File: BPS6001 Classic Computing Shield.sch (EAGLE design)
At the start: 82 parts, among them IC1 MAX3232CSE, X1 VGA

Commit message: First outline of design moved to Eagle 9.
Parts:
- removed AJ1: AUDIO-CONNECTOR-6P-SMD-3440030P1, OPL Eagle Library:AUDIO-CONNECTOR-6P-SMD-3440030P1
- removed C4, C5, C6, C7: .1uF, GadgetFactory_6.0:C0805
- removed GROVE1: (no value), GadgetFactory_6.0:CONNECTOR_TWIG-2.0-LEADED
- removed IC1: MAX3232CSE, maxim:MAX3232CSE
- removed PS2_A: MINI-DIN6PTH, SparkFun-Connectors:MINI-DIN6PTH
- removed SP1: Serial Port, con-subd:M09HP
- added B1: SPARKFUN_LOGIC_LEVEL_CONVERTER, SparkFun-Boards:SPARKFUN_LOGIC_LEVEL_CONVERTER
- added R49, R50, R51: 1k, resistor:R-EU_R0603
- added X2: MAB6H, con-hirschmann:MAB6H
- C1, C2: value 4700pF -> 10p; device GadgetFactory:C0603 -> resistor:C-EUC0603; PARTNO C0603C472J5RACTU -> (none)
- C3: value .1uF -> 10p; device GadgetFactory_6.0:C0805 -> resistor:C-EUC0603; PARTNO GRM21BR71E104KA01L -> (none)
- R22, R28: value 3.3K -> 1k; device GadgetFactory:R0603 -> resistor:R-EU_R0603; PARTNO RMCF0603JT3K30 -> (none)
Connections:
- removed net 3V3: C7.1, CFG1.10, CFG1.2, CFG1.4, CFG1.6, CFG1.8, H1.3.3V, IC1P.VCC, R1A.2, R23A.2, R24A.2, R25A.2, R2A.2, R3A.2, R4A.2, R5A.2, R6A.2, R7A.2, R8A.2, S1.S1, S2.S1, S3.S1, S4.S1, S5.S1, SD1.VDD
- removed net AUDIO1-LEFT: H1.D28, R22A.2
- removed net AUDIO1-RIGHT: H1.D30, R28A.2
- removed net CTS: IC1G$1.R2OUT
- removed net DTE_CTS: IC1G$1.R2IN, SP1.8
- removed net DTE_RTS: IC1G$1.T2OUT, SP1.7
- removed net DTE_RX: IC1G$1.R1IN, SP1.2
- removed net DTE_TX: IC1G$1.T1OUT, SP1.3
- removed net N$12: C4.2, IC1G$1.C2+
- removed net N$13: C5.1, IC1G$1.C1-
- removed net N$14: C4.1, IC1G$1.C2-
- removed net N$2: AJ1.L, C1.1, R22A.1
- removed net N$34: AJ1.R, C2.1, R28A.1
- removed net N$6: C6.1, IC1G$1.V+
- removed net N$7: C3.1, IC1G$1.V-
- removed net N$8: C5.2, IC1G$1.C1+
- removed net PS2CLK1: H1.D5, PS2_A.5
- removed net PS2DAT1: H1.D4, PS2_A.1
- removed net RTS: IC1G$1.T2IN
- new net 3V3_PWR6: B1.LV, C3.2, CFG1.10, CFG1.2, CFG1.4, CFG1.6, CFG1.8, H1.3.3V, R1A.2, R23A.2, R24A.2, R25A.2, R2A.2, R3A.2, R4A.2, R5A.2, R6A.2, R7A.2, R8A.2, S1.S, S1.S1, S2.S, S2.S1, S3.S, S3.S1, S4.S, S4.S1, S5.S1, SD1.VDD
- new net 3V3_PWR7: PWR_2.3V3@P3
- new net IEC-H-ATN: B1.HV_TXO_1, C2.2, R28.1, X2.3
- new net IEC-H-CLK: B1.HV_RXI_1, R49.1, X2.4
- new net IEC-H-DATA: B1.HV_RXI_2, R50.1, X2.5
- new net IEC-H-RESET: B1.HV_TXO_2, R51.1, X2.6
- new net IEC-H-SRQ: R22.1, X2.1
- new net IEC-L-ATN: B1.LV_TXI_1, H1.D28
- new net IEC-L-CLK: B1.LV_RXO_1, H1.D4
- new net IEC-L-DATA: B1.LV_RXO_2, H1.D5
- new net IEC-L-RESET: B1.LV_TXI_2, H1.D30
- net 5V0: now also B1.HV, C1.1, R22.2, R28.2, R49.2, R50.2, R51.2; no longer GROVE1.3, PS2_A.4
- net GND: now also B1.GND, B1.GND@2, C2.1, C3.1, X2.2, X2.PE; no longer AJ1.COM1, AJ1.COM2, C2.2, C3.2, C6.2, C7.2, GROVE1.4, IC1P.GND, PS2_A.3, SP1.5, SP1.G1, SP1.G2
- net JS1_5: no longer GROVE1.2
- net JS1_9: no longer GROVE1.1
- net RX: no longer IC1G$1.R1OUT
- net TX: no longer IC1G$1.T1IN
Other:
- note removed: "Seeed Grove Connector"

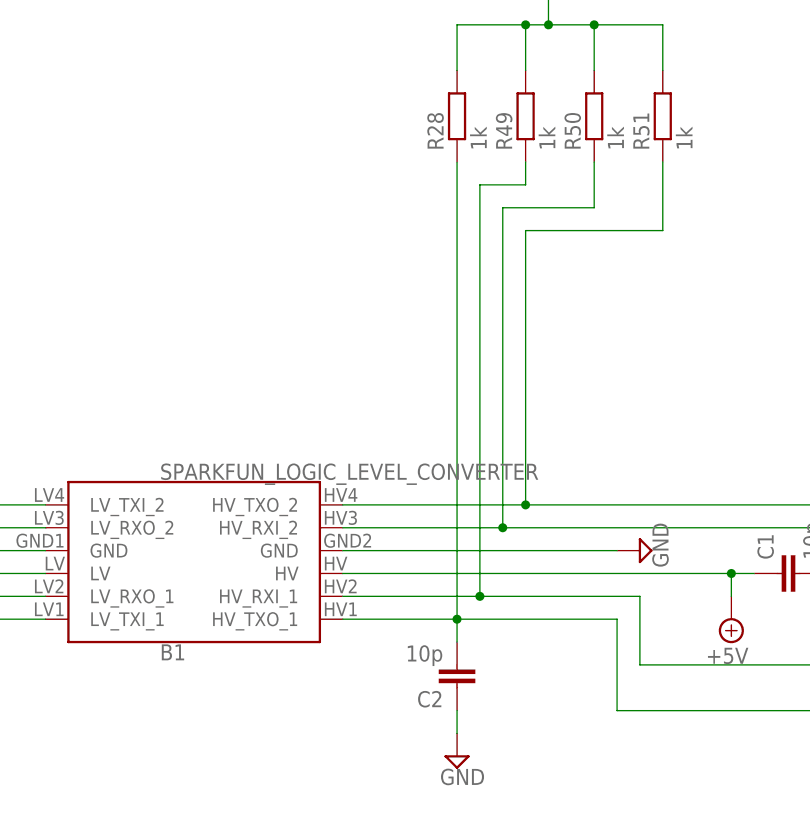
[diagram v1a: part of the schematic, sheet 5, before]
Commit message: Fixed some issues, board is now without problems.
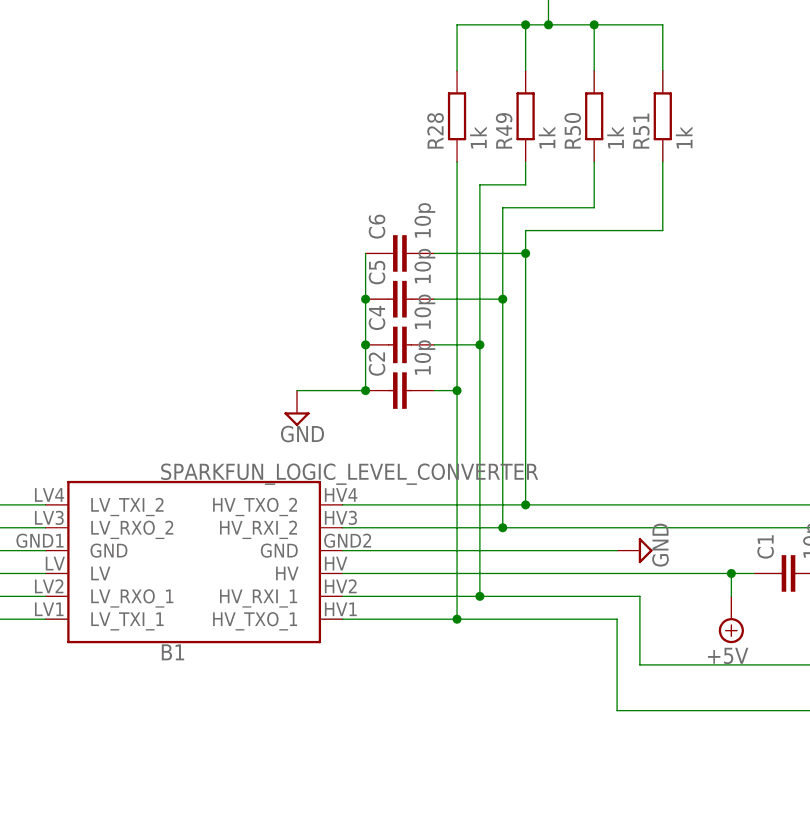
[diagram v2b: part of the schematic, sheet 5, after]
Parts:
- added C4, C5, C6: 10p, resistor:C-EUC0603
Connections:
- net GND: now also C4.1, C5.1, C6.1
- net IEC-H-CLK: now also C4.2
- net IEC-H-DATA: now also C5.2
- net IEC-H-RESET: now also C6.2
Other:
- moved on the sheet: C2
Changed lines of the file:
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@@
 <part name="3V3_PWR12" library="GadgetFactory" deviceset="3V3" device=""/>
 <part name="SUPPLY14" library="supply2" library_urn="urn:adsk.eagle:library:372" deviceset="+5V" device=""/>
+<part name="C4" library="resistor" deviceset="C-EU" device="C0603" value="10p"/>
+<part name="C5" library="resistor" deviceset="C-EU" device="C0603" value="10p"/>
+<part name="C6" library="resistor" deviceset="C-EU" device="C0603" value="10p"/>
 </parts>
 <sheets>
@@
 <attribute name="VALUE" x="135.255" y="180.975" size="1.778" layer="96"/>
 </instance>
-<instance part="C2" gate="G$1" x="127" y="96.52" smashed="yes" rot="R180">
-<attribute name="NAME" x="125.476" y="96.139" size="1.778" layer="95" rot="R180"/>
-<attribute name="VALUE" x="125.476" y="101.219" size="1.778" layer="96" rot="R180"/>
-</instance>
-<instance part="SUPPLY13" gate="GND" x="127" y="88.9" smashed="yes">
-<attribute name="VALUE" x="125.095" y="85.725" size="1.778" layer="96"/>
+<instance part="C2" gate="G$1" x="119.38" y="129.54" smashed="yes" rot="R90">
+<attribute name="NAME" x="118.999" y="131.064" size="1.778" layer="95" rot="R90"/>
+<attribute name="VALUE" x="124.079" y="131.064" size="1.778" layer="96" rot="R90"/>
+</instance>
+<instance part="SUPPLY13" gate="GND" x="109.22" y="127" smashed="yes">
+<attribute name="VALUE" x="107.315" y="123.825" size="1.778" layer="96"/>
 </instance>
 <instance part="C3" gate="G$1" x="38.1" y="104.14" smashed="yes" rot="R180">
@@
 <instance part="SUPPLY14" gate="+5V" x="236.22" y="109.22" smashed="yes" rot="R180">
 <attribute name="VALUE" x="238.125" y="106.045" size="1.778" layer="96" rot="R180"/>
+</instance>
+<instance part="C4" gate="G$1" x="119.38" y="134.62" smashed="yes" rot="R90">
+<attribute name="NAME" x="118.999" y="136.144" size="1.778" layer="95" rot="R90"/>
+<attribute name="VALUE" x="124.079" y="136.144" size="1.778" layer="96" rot="R90"/>
+</instance>
+<instance part="C5" gate="G$1" x="119.38" y="139.7" smashed="yes" rot="R90">
+<attribute name="NAME" x="118.999" y="141.224" size="1.778" layer="95" rot="R90"/>
+<attribute name="VALUE" x="124.079" y="141.224" size="1.778" layer="96" rot="R90"/>
+</instance>
+<instance part="C6" gate="G$1" x="119.38" y="144.78" smashed="yes" rot="R90">
+<attribute name="NAME" x="118.999" y="146.304" size="1.778" layer="95" rot="R90"/>
+<attribute name="VALUE" x="124.079" y="146.304" size="1.778" layer="96" rot="R90"/>
 </instance>
 </instances>
@@
 <pinref part="R51" gate="G$1" pin="1"/>
 <wire x1="149.86" y1="154.94" x2="149.86" y2="147.32" width="0.1524" layer="91"/>
-<wire x1="134.62" y1="147.32" x2="134.62" y2="116.84" width="0.1524" layer="91"/>
+<wire x1="134.62" y1="147.32" x2="134.62" y2="144.78" width="0.1524" layer="91"/>
 <junction x="134.62" y="116.84"/>
+<pinref part="C6" gate="G$1" pin="2"/>
+<wire x1="134.62" y1="144.78" x2="134.62" y2="116.84" width="0.1524" layer="91"/>
+<wire x1="124.46" y1="144.78" x2="134.62" y2="144.78" width="0.1524" layer="91"/>
+<junction x="134.62" y="144.78"/>
 </segment>
 </net>
@@
 <wire x1="142.24" y1="154.94" x2="142.24" y2="149.86" width="0.1524" layer="91"/>
 <wire x1="142.24" y1="149.86" x2="132.08" y2="149.86" width="0.1524" layer="91"/>
-<wire x1="132.08" y1="149.86" x2="132.08" y2="114.3" width="0.1524" layer="91"/>
+<wire x1="132.08" y1="149.86" x2="132.08" y2="139.7" width="0.1524" layer="91"/>
 <junction x="132.08" y="114.3"/>
+<pinref part="C5" gate="G$1" pin="2"/>
+<wire x1="132.08" y1="139.7" x2="132.08" y2="114.3" width="0.1524" layer="91"/>
+<wire x1="124.46" y1="139.7" x2="132.08" y2="139.7" width="0.1524" layer="91"/>
+<junction x="132.08" y="139.7"/>
 </segment>
 </net>
@@
 <wire x1="218.44" y1="106.68" x2="210.82" y2="106.68" width="0.1524" layer="91"/>
 <pinref part="R28" gate="G$1" pin="1"/>
-<wire x1="127" y1="154.94" x2="127" y2="104.14" width="0.1524" layer="91"/>
+<wire x1="127" y1="154.94" x2="127" y2="129.54" width="0.1524" layer="91"/>
 <junction x="127" y="104.14"/>
 <pinref part="C2" gate="G$1" pin="2"/>
-<wire x1="127" y1="104.14" x2="127" y2="101.6" width="0.1524" layer="91"/>
+<wire x1="127" y1="129.54" x2="127" y2="104.14" width="0.1524" layer="91"/>
+<wire x1="124.46" y1="129.54" x2="127" y2="129.54" width="0.1524" layer="91"/>
+<junction x="127" y="129.54"/>
 </segment>
 </net>
@@
 <wire x1="134.62" y1="154.94" x2="134.62" y2="152.4" width="0.1524" layer="91"/>
 <wire x1="134.62" y1="152.4" x2="129.54" y2="152.4" width="0.1524" layer="91"/>
-<wire x1="129.54" y1="152.4" x2="129.54" y2="106.68" width="0.1524" layer="91"/>
+<wire x1="129.54" y1="152.4" x2="129.54" y2="134.62" width="0.1524" layer="91"/>
 <junction x="129.54" y="106.68"/>
+<pinref part="C4" gate="G$1" pin="2"/>
+<wire x1="129.54" y1="134.62" x2="129.54" y2="106.68" width="0.1524" layer="91"/>
+<wire x1="124.46" y1="134.62" x2="129.54" y2="134.62" width="0.1524" layer="91"/>
+<junction x="129.54" y="134.62"/>
 </segment>
 </net>
@@
 <pinref part="C2" gate="G$1" pin="1"/>
 <pinref part="SUPPLY13" gate="GND" pin="GND"/>
-<wire x1="127" y1="93.98" x2="127" y2="91.44" width="0.1524" layer="91"/>
-</segment>
-</net>
+<wire x1="116.84" y1="129.54" x2="109.22" y2="129.54" width="0.1524" layer="91"/>
+<pinref part="C6" gate="G$1" pin="1"/>
+<pinref part="C5" gate="G$1" pin="1"/>
+<wire x1="116.84" y1="144.78" x2="116.84" y2="139.7" width="0.1524" layer="91"/>
+<pinref part="C4" gate="G$1" pin="1"/>
+<wire x1="116.84" y1="139.7" x2="116.84" y2="134.62" width="0.1524" layer="91"/>
+<junction x="116.84" y="139.7"/>
+<wire x1="116.84" y1="134.62" x2="116.84" y2="129.54" width="0.1524" layer="91"/>
+<junction x="116.84" y="134.62"/>
+<junction x="116.84" y="129.54"/>
+</segment>
+</net>
